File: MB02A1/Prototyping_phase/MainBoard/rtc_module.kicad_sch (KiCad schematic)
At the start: 8 parts, among them U10 MCP7940N-xSN, X4 32.768 kHz

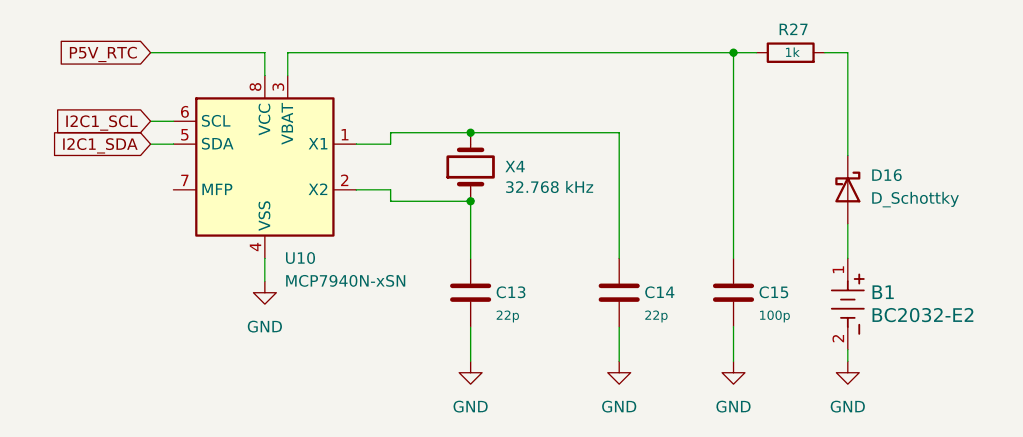
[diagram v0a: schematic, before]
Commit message: Datasheets added, design updated.
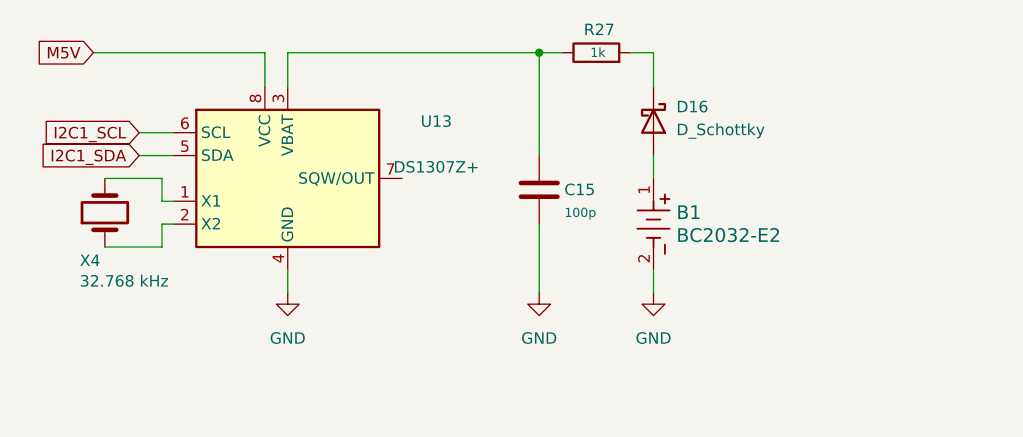
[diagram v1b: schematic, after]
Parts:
- removed C13, C14: 22p, Capacitor_SMD:C_0805_2012Metric, symbol Device:C
- removed U10: MCP7940N-xSN, Package_SO:SOIC-8_3.9x4.9mm_P1.27mm, symbol Timer_RTC:MCP7940N-xSN
- added U13: DS1307Z+, Package_SO:SOIC-8_3.9x4.9mm_P1.27mm, symbol Timer_RTC:DS1307Z+
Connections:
- net GND: now also U13.4 (GND)
- net I2C1_SCL: now also U13.6 (SCL)
- net I2C1_SDA: now also U13.5 (SDA)
- net at X4.1: now also U13.2 (X2)
- net at X4.2: now also U13.1 (X1)
- net at C15.1, R27.1: now also U13.3 (VBAT)
- new net M5V: U13.8 (VCC)
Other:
- moved on the sheet: B1, C15, D16, R27

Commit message: Design update, production preparation.
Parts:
- removed C15: 100p, Capacitor_SMD:C_0805_2012Metric, symbol Device:C
- removed D16: D_Schottky, Diode_SMD:D_1206_3216Metric, symbol Device:D_Schottky
- removed R27: 1k, Resistor_SMD:R_0805_2012Metric, symbol Device:R
- removed U13: DS1307Z+, Package_SO:SOIC-8_3.9x4.9mm_P1.27mm, symbol Timer_RTC:DS1307Z+
- removed X4: 32.768 kHz, Crystal:Crystal_HC18-U_Vertical, symbol Device:Crystal
- added U11: DS3231M, Package_SO:SOIC-16W_7.5x10.3mm_P1.27mm, symbol Timer_RTC:DS3231M
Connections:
- net GND: now also U11.10 (GND), U11.11 (GND), U11.12 (GND), U11.13 (GND), U11.5 (GND), U11.6 (GND), U11.7 (GND), U11.8 (GND), U11.9 (GND)
- net I2C1_SCL: now also U11.16 (SCL)
- net I2C1_SDA: now also U11.15 (SDA)
- net M5V: now also U11.2 (VCC)
- net at B1.1: now also U11.14 (VBAT)
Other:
- moved on the sheet: B1
